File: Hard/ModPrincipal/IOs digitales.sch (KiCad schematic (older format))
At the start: 25 parts

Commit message: Asignacion inicial de footprints
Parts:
- removed C?: 1nF, Capacitor_SMD:C_0805_2012Metric_Pad1.15x1.40mm_HandSolder, symbol pspice:C
- removed D? (x2): 1N4148W, Diode_SMD:D_SOD-123, symbol Diode:1N4148W
- removed D?: 1N5242, Diode_THT:D_DO-35_SOD27_P7.62mm_Horizontal, symbol Device:D_Zener
- removed R?: 5.6k, Resistor_THT:R_Axial_DIN0207_L6.3mm_D2.5mm_P10.16mm_Horizontal, symbol Device:R
- removed R?: 4.7k, Resistor_THT:R_Axial_DIN0207_L6.3mm_D2.5mm_P10.16mm_Horizontal, symbol Device:R
- added C701, C702: 1nF, Capacitor_SMD:C_0805_2012Metric_Pad1.15x1.40mm_HandSolder, symbol pspice:C
- added D703, D704, D705, D706: 1N4148W, Diode_SMD:D_MiniMELF_Handsoldering, symbol Diode:1N4148W
- added R709, R710: 10k, Resistor_SMD:R_0805_2012Metric_Pad1.15x1.40mm_HandSolder, symbol Device:R
- added R712, R713, R714: 1M, Resistor_SMD:R_0805_2012Metric_Pad1.15x1.40mm_HandSolder, symbol Device:R
- added R715, R716, R717: 470, Resistor_SMD:R_0805_2012Metric_Pad1.15x1.40mm_HandSolder, symbol Device:R
- D707, D708: renamed from D?; footprint Diode_SMD:D_SOD-123 -> Diode_SMD:D_MiniMELF_Handsoldering
- R711: renamed from R?; footprint Resistor_THT:R_Axial_DIN0207_L6.3mm_D2.5mm_P10.16mm_Horizontal -> Resistor_SMD:R_0805_2012Metric_Pad1.15x1.40mm_HandSolder
- gave numbers to parts that had none: 16
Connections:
- net labels added: CPU_In2, Entrada2
- wire segments 72 -> 90
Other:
- note removed: "En este punto el\nzener limita a 12v"

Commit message: Asignación de footprint y corrección de errores de ERC en esquematico
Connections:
- no-connect marks 0 -> 2
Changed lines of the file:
@@
 EESchema Schematic File Version 4
-LIBS:ModPrincipal-cache
 EELAYER 30 0
 EELAYER END
@@
 Wire Wire Line
 	7950 5900 7950 6000
+NoConn ~ 3550 5700
+NoConn ~ 3150 5700
 $EndSCHEMATC

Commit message: Avance en place de componentes
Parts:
- removed K701: RT42xxxx, Relay_THT:Relay_DPDT_Schrack-RT2-FormC_RM5mm, symbol Relay:RT42xxxx
- added K701: RT44xxxx, Relay_THT:Relay_DPST_Schrack-RT2-FormA_RM5mm, symbol Relay:RT44xxxx
- D703, D704, D705, D706, D707, D708: footprint Diode_SMD:D_MiniMELF_Handsoldering -> Diode_SMD:D_MiniMELF
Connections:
- no-connect marks 2 -> 0
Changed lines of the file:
@@
 EESchema Schematic File Version 4
-LIBS:ModPrincipal-cache
 EELAYER 30 0
 EELAYER END
@@
 F 0 "D708" V 9004 1880 50  0000 L CNN
 F 1 "1N4148W" V 9095 1880 50  0000 L CNN
-F 2 "Diode_SMD:D_MiniMELF_Handsoldering" H 9050 1625 50  0001 C CNN
+F 2 "Diode_SMD:D_MiniMELF" H 9050 1625 50  0001 C CNN
 F 3 "https://www.vishay.com/docs/85748/1n4148w.pdf" H 9050 1800 50  0001 C CNN
 	1    9050 1800
@@
 F 0 "D707" V 9004 1380 50  0000 L CNN
 F 1 "1N4148W" V 9095 1380 50  0000 L CNN
-F 2 "Diode_SMD:D_MiniMELF_Handsoldering" H 9050 1125 50  0001 C CNN
+F 2 "Diode_SMD:D_MiniMELF" H 9050 1125 50  0001 C CNN
 F 3 "https://www.vishay.com/docs/85748/1n4148w.pdf" H 9050 1300 50  0001 C CNN
 	1    9050 1300
@@
 Wire Wire Line
 	1900 7150 1900 7300
-$Comp
-L Relay:RT42xxxx K701
-U 1 1 5EFA37ED
-P 3250 6000
-F 0 "K701" H 3880 6046 50  0000 L CNN
-F 1 "RT42xxxx" H 3880 5955 50  0000 L CNN
-F 2 "Relay_THT:Relay_DPDT_Schrack-RT2-FormC_RM5mm" H 3250 6000 50  0001 C CNN
-F 3 "http://www.te.com/commerce/DocumentDelivery/DDEController?Action=showdoc&DocId=Data+Sheet%7FRT2%7F1014%7Fpdf%7FEnglish%7FENG_DS_RT2_1014.pdf%7F6-1393243-3" H 3250 6000 50  0001 C CNN
-	1    3250 6000
-	1    0    0    -1
-$EndComp
 Wire Wire Line
 	2850 6300 2850 6350
@@
 Wire Wire Line
 	2850 6950 2850 7000
-Wire Wire Line
-	4450 5100 3350 5100
-Wire Wire Line
-	3350 5100 3350 5700
-Wire Wire Line
-	3750 5700 3750 5500
-Wire Wire Line
-	3750 5500 4450 5500
-Text HLabel 4450 6900 2    50   Output ~ 0
+Text HLabel 4100 5100 2    50   Output ~ 0
 L_220V_Out
-Text HLabel 4450 6500 2    50   Output ~ 0
+Text HLabel 4100 5500 2    50   Output ~ 0
 N_220V_Out
-Wire Wire Line
-	4450 6500 3650 6500
-Wire Wire Line
-	3650 6500 3650 6300
-Wire Wire Line
-	3250 6300 3250 6900
-Wire Wire Line
-	3250 6900 4450 6900
-Text GLabel 4450 5100 2    50   Input ~ 0
+Text GLabel 4100 6900 2    50   Input ~ 0
 L_220VAC
-Text GLabel 4450 5500 2    50   Input ~ 0
+Text GLabel 4100 6500 2    50   Input ~ 0
 N_220VAC
 $Comp
@@
 F 0 "D704" V 8654 4030 50  0000 L CNN
 F 1 "1N4148W" V 8745 4030 50  0000 L CNN
-F 2 "Diode_SMD:D_MiniMELF_Handsoldering" H 8700 3775 50  0001 C CNN
+F 2 "Diode_SMD:D_MiniMELF" H 8700 3775 50  0001 C CNN
 F 3 "https://www.vishay.com/docs/85748/1n4148w.pdf" H 8700 3950 50  0001 C CNN
 	1    8700 3950
@@
 F 0 "D703" V 8654 3530 50  0000 L CNN
 F 1 "1N4148W" V 8745 3530 50  0000 L CNN
-F 2 "Diode_SMD:D_MiniMELF_Handsoldering" H 8700 3275 50  0001 C CNN
+F 2 "Diode_SMD:D_MiniMELF" H 8700 3275 50  0001 C CNN
 F 3 "https://www.vishay.com/docs/85748/1n4148w.pdf" H 8700 3450 50  0001 C CNN
 	1    8700 3450
@@
 F 0 "D706" V 8654 5730 50  0000 L CNN
 F 1 "1N4148W" V 8745 5730 50  0000 L CNN
-F 2 "Diode_SMD:D_MiniMELF_Handsoldering" H 8700 5475 50  0001 C CNN
+F 2 "Diode_SMD:D_MiniMELF" H 8700 5475 50  0001 C CNN
 F 3 "https://www.vishay.com/docs/85748/1n4148w.pdf" H 8700 5650 50  0001 C CNN
 	1    8700 5650
@@
 F 0 "D705" V 8654 5230 50  0000 L CNN
 F 1 "1N4148W" V 8745 5230 50  0000 L CNN
-F 2 "Diode_SMD:D_MiniMELF_Handsoldering" H 8700 4975 50  0001 C CNN
+F 2 "Diode_SMD:D_MiniMELF" H 8700 4975 50  0001 C CNN
 F 3 "https://www.vishay.com/docs/85748/1n4148w.pdf" H 8700 5150 50  0001 C CNN
 	1    8700 5150
@@
 Wire Wire Line
 	7950 5900 7950 6000
-NoConn ~ 3550 5700
-NoConn ~ 3150 5700
+Wire Wire Line
+	4100 5500 3750 5500
+Wire Wire Line
+	3750 5500 3750 5700
+Wire Wire Line
+	4100 5100 3350 5100
+Wire Wire Line
+	3350 5100 3350 5700
+Wire Wire Line
+	3650 6300 3650 6500
+Wire Wire Line
+	3650 6500 4100 6500
+Wire Wire Line
+	4100 6900 3250 6900
+Wire Wire Line
+	3250 6900 3250 6300
+$Comp
+L Relay:RT44xxxx K701
+U 1 1 5ED8A7A8
+P 3250 6000
+F 0 "K701" H 3880 6046 50  0000 L CNN
+F 1 "RT44xxxx" H 3880 5955 50  0000 L CNN
+F 2 "Relay_THT:Relay_DPST_Schrack-RT2-FormA_RM5mm" H 3250 6000 50  0001 C CNN
+F 3 "http://www.te.com/commerce/DocumentDelivery/DDEController?Action=showdoc&DocId=Data+Sheet%7FRT2%7F1014%7Fpdf%7FEnglish%7FENG_DS_RT2_1014.pdf%7F6-1393243-3" H 3250 6000 50  0001 C CNN
+	1    3250 6000
+	1    0    0    -1
+$EndComp
 $EndSCHEMATC

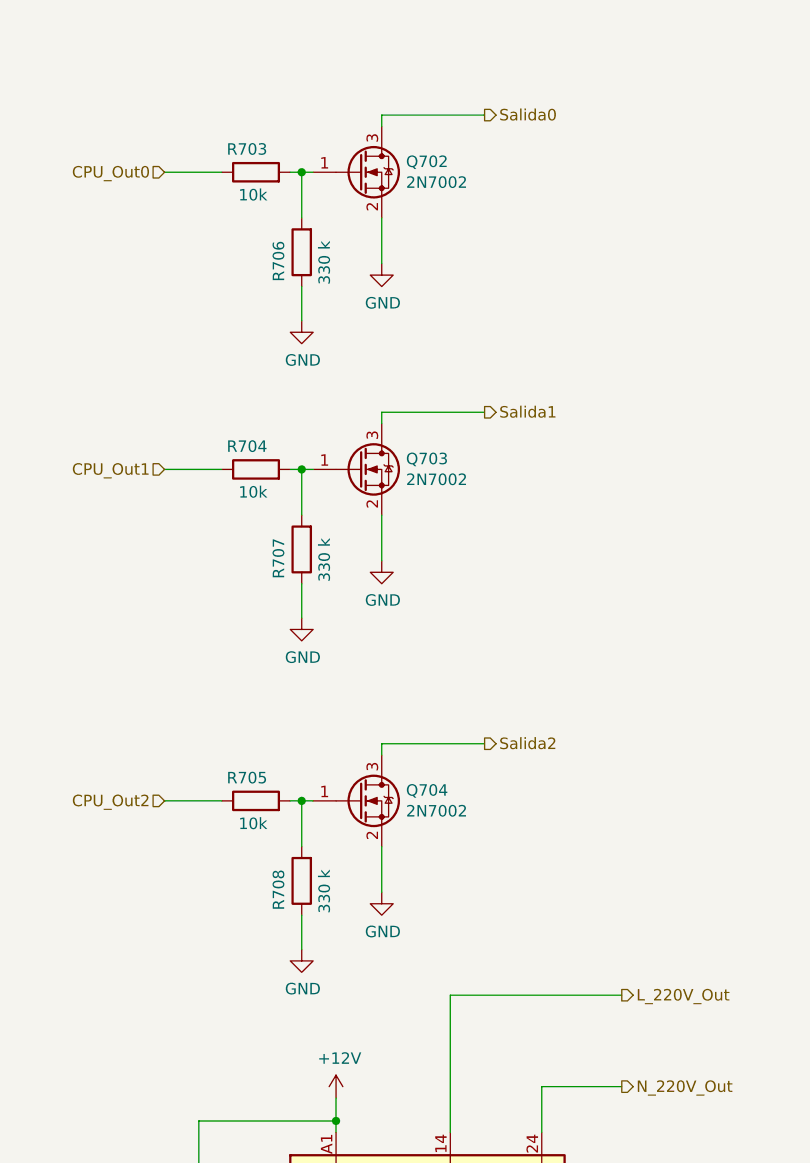
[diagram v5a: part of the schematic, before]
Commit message: Primera correccion en modulos Adicionales y cambio de etapa de salida en modulo principal
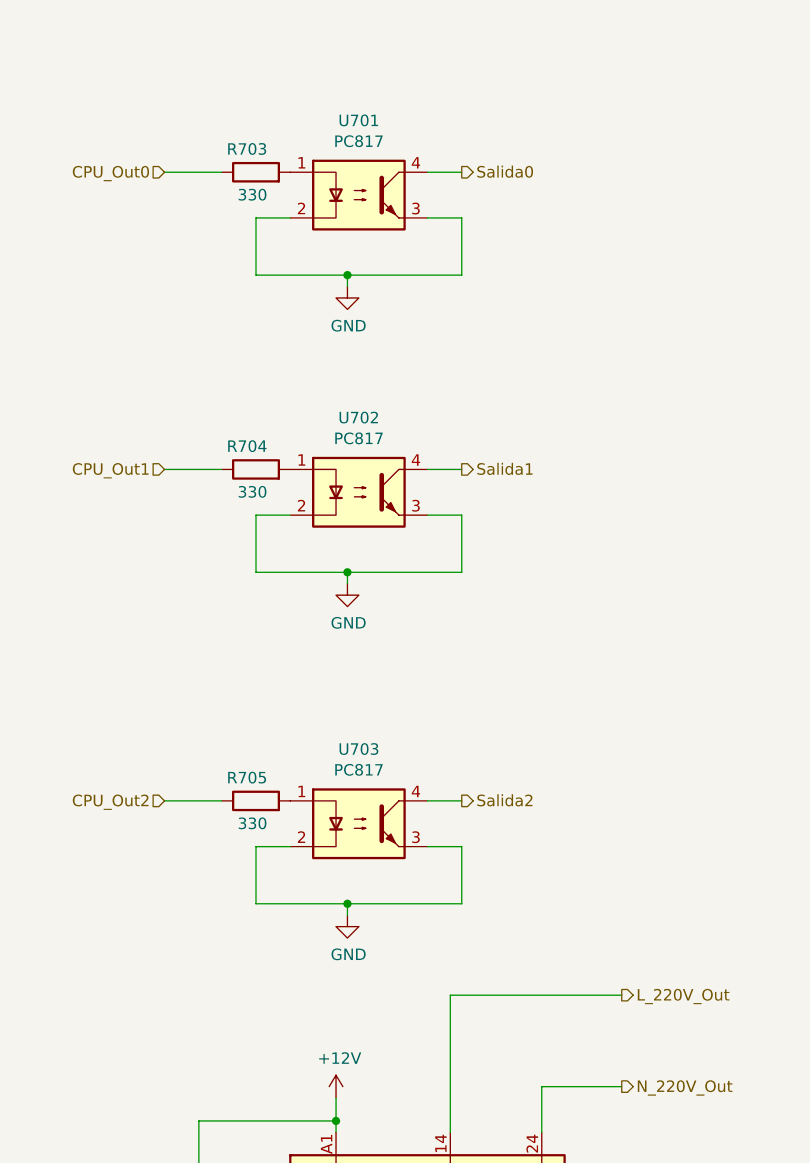
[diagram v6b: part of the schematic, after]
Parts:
- removed Q702, Q703, Q704: 2N7002, Package_TO_SOT_SMD:SOT-23, symbol Transistor_FET:2N7002
- removed R706, R707, R708: 330 k, Resistor_SMD:R_0805_2012Metric_Pad1.15x1.40mm_HandSolder, symbol Device:R
- added U701, U702, U703: PC817, Package_SO:SO-4_7.6x3.6mm_P2.54mm, symbol Isolator:PC817
- R703, R704, R705: value 10k -> 330
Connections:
- net GND: now also U701.2, U701.3, U702.2, U702.3, U703.2, U703.3
- net Salida0: now also U701.4
- net Salida1: now also U702.4
- net Salida2: now also U703.4
- net at R703.2: now also U701.1
- net at R704.2: now also U702.1
- net at R705.2: now also U703.1
